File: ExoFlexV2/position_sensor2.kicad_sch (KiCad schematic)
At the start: 24 parts

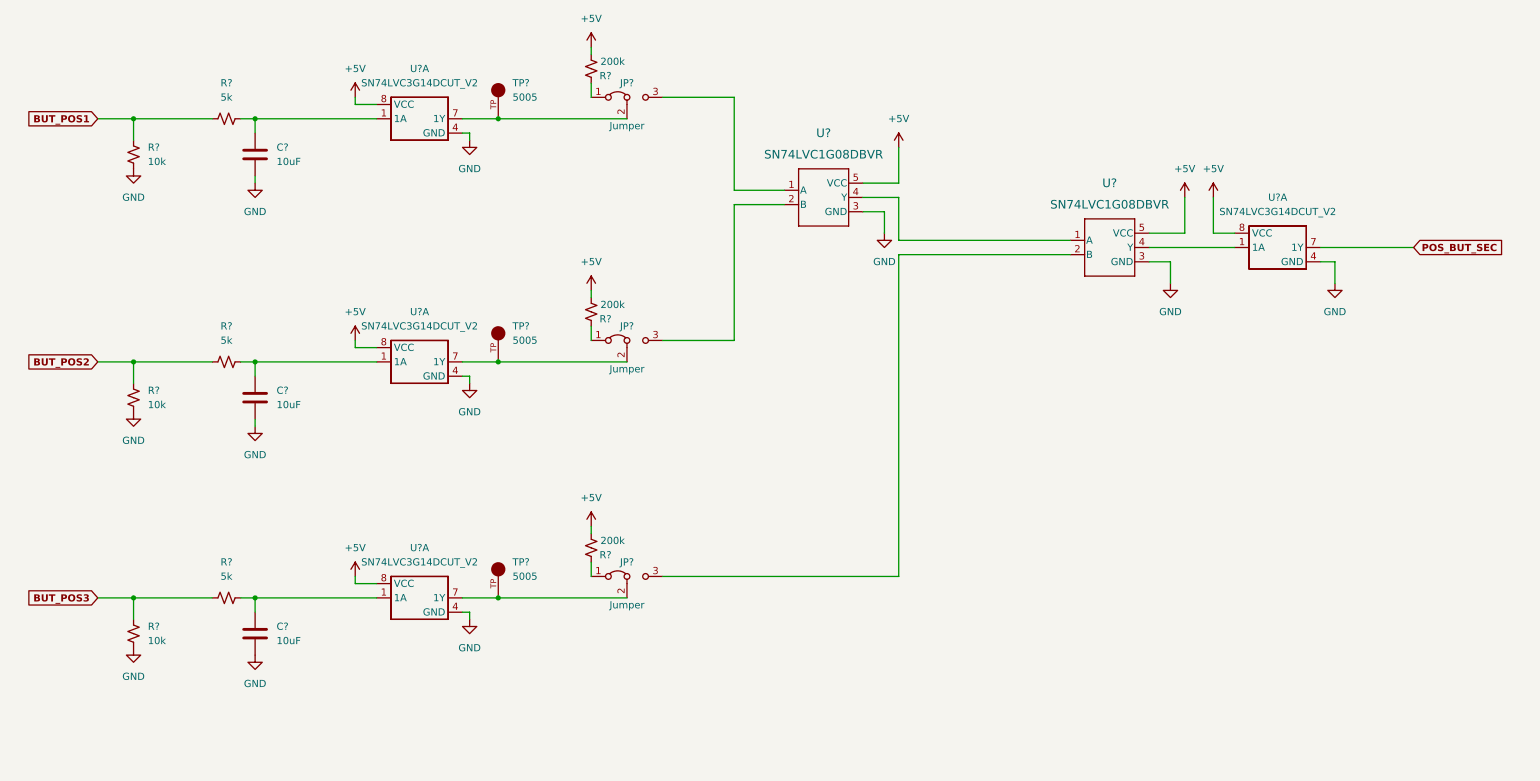
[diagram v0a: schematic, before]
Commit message: Mise à jour signaux STM
- Condo de découplage
- Signaux supplémentaire pour le STM
- Page GND sera pour Multiplexeur
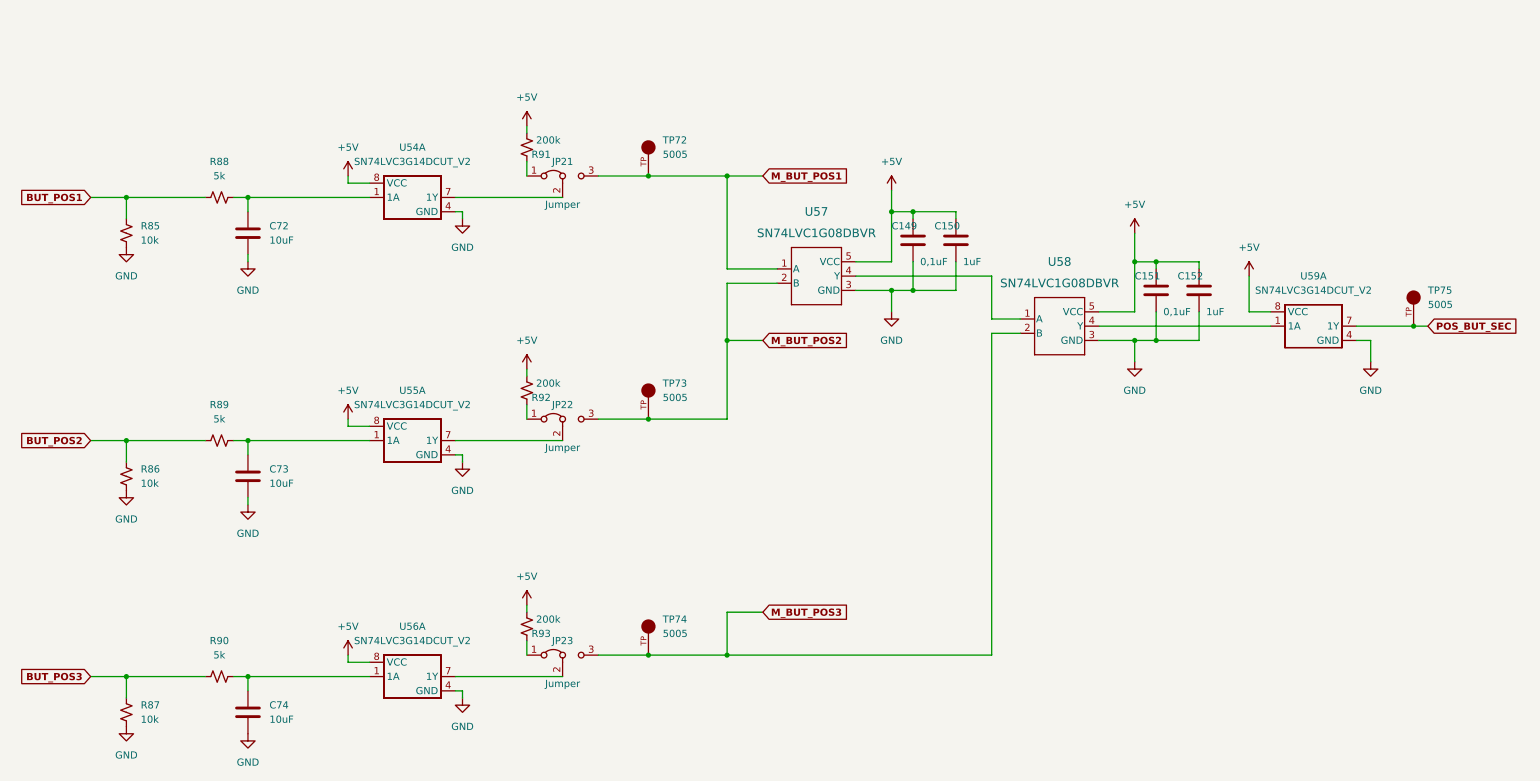
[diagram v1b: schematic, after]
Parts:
- removed TP? (x3): 5005, FootPrint:KEYSTONE_5005, symbol SymLib:5005
- added C149, C151: 0,1uF, Capacitor_SMD:C_0603_1608Metric, symbol Device:C
- added C150, C152: 1uF, Capacitor_SMD:C_0603_1608Metric, symbol Device:C
- added TP72, TP73, TP74, TP75: 5005, FootPrint:KEYSTONE_5005, symbol SymLib:5005
- gave numbers to parts that had none: 21
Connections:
- net +5V: now also C149.1, C150.1, C151.1, C152.1
- net GND: now also C149.2, C150.2, C151.2, C152.2
- net POS_BUT_SEC: now also TP75.TP
- net M_BUT_POS3: now reaches JP23.3 (B), U58.2 (B)
- net M_BUT_POS3: now also TP74.TP
- net M_BUT_POS2: now reaches JP22.3 (B), U57.2 (B)
- net M_BUT_POS2: now also TP73.TP
- net M_BUT_POS1: now reaches JP21.3 (B), U57.1 (A)
- net M_BUT_POS1: now also TP72.TP
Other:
- moved on the sheet: C72, C73, C74, JP21, JP22, JP23, R85, R86, R87, R88, R89, R90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

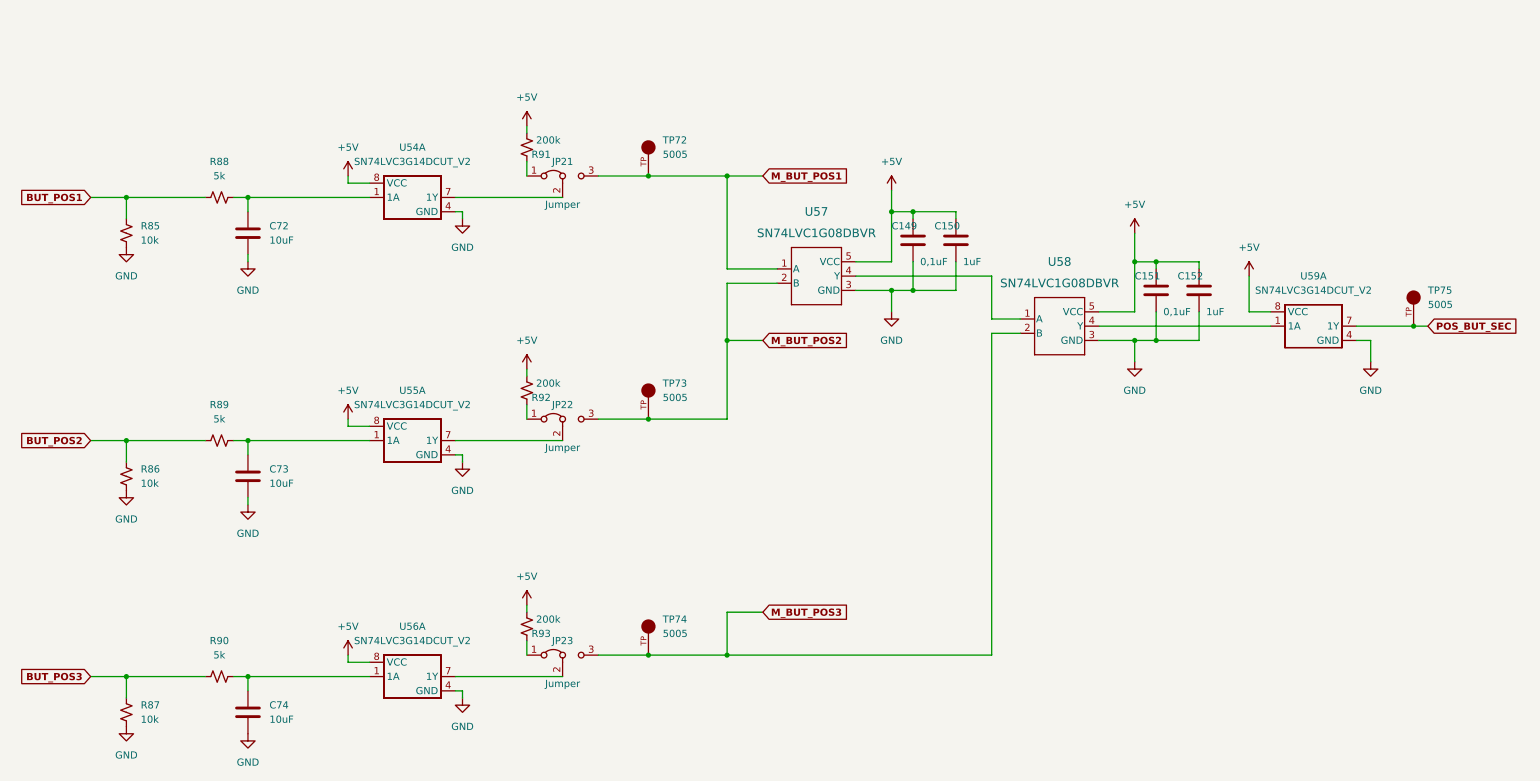
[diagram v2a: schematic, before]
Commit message: Finalisation 1
- Ajout de pages pour la gestion des signaux négatif
- Modification des pages de torque et amplitude
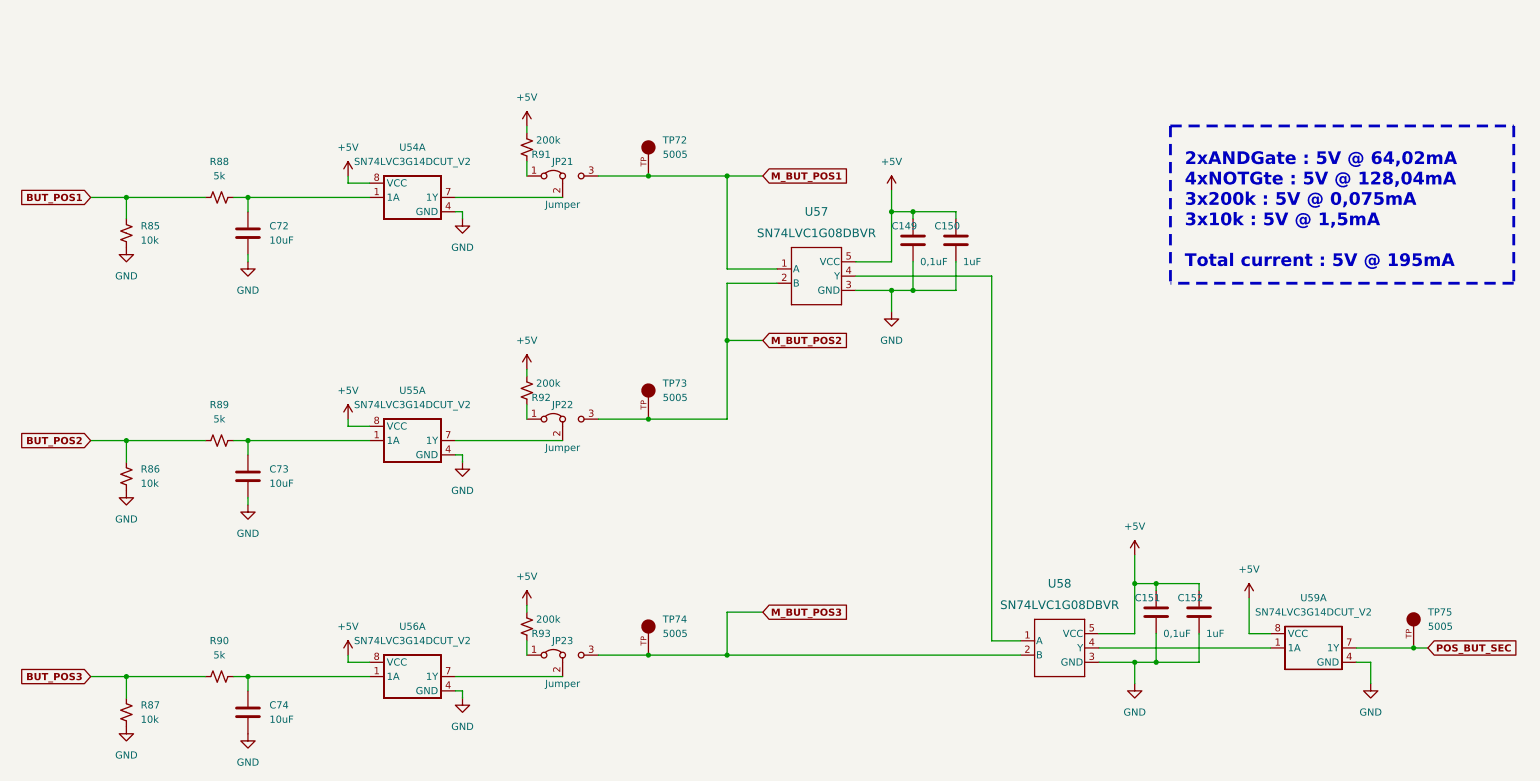
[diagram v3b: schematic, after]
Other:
- note added: "2xANDGate : 5V @ 64,02mA 4xNOTGte : 5V @ 128,04mA 3x200k : 5V @ 0,075mA 3x10k : 5V @ 1,5mA Total current : 5V @ 195mA"
- moved on the sheet: C151, C152, TP75, U58, U59A
